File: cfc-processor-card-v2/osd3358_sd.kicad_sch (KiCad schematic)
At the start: 98 parts, among them J100 DM3BT-DSF-PEJS, J3 CONN_03LONGPADS, U11 TCAN330, U17 25AAXX, U2 DS90CR218AMTD/NOPBMTD48_TEX-L, U3 THGBMJG7C2LBAU8, U7 OSD3358-512M-BSM

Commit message: Clean up CFC Processor Card from Scott's initial import which was Gerber identical to origianl EAGLE schematic. Interestingly, this version was already changed for the v2 backplane which is great. Align schematic to be more KiCAD like based off of the C3, rename a few things, remove some outdated OPD connections, import sch into pcb, clean up pcb detritus, and import DRU settings. No longer Gerber identicial, but it's now ready for further polishing for fabrication.
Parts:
- removed J3: CONN_03LONGPADS, cfc-card:1X03_LONGPADS, symbol cfc-card-eagle-import:CONN_03LONGPADS
- removed JP2: JUMPER-SMT_3_1-NC_TRACE_SILK, cfc-card:SMT-JUMPER_3_1-NC_TRACE_SILK, symbol cfc-card-eagle-import:JUMPER-SMT_3_1-NC_TRACE_SILK
- removed R14: DNP, cfc-card:.0603-A, symbol cfc-card-eagle-import:R-US_0603-A
- removed R16, R17: 100k, cfc-card:RES_EXB2HV, symbol cfc-card-eagle-import:EXB-2HV103JV
- removed SB0, SB1, SB10, SB11, SB12, SB13, SB14, SB15, SB2, SB3, SB4, SB5, SB6, SB7, SB8, SB9: TEST-POINT-SMALL, cfc-card:TEST-POINT-SMALL, symbol cfc-card-eagle-import:TEST-POINT-SMALL
- removed unit 4 of U7
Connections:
- no-connect marks 64 -> 44
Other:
- note removed: "Boot SD SYSBOOT[4 : 0] == 0b11000 SPI0 -> MMC0 -> USB0 -> UART0 Boot eMMC SYSBOOT[4 : 0] == 0b11100 MMC1 -> MMC0 -> UART0 -> USB0"
- note removed: "Default Sysboot Pins SYSBOOT[4 : 0] == 0b11x00 SYSBOOT[2] HIGH == eMMC SYSBOOT[2] LOW == SD Card"
- note removed: "PIRT1280 Enable and TEC enable GPIO. We are using these pins because they are free and are the ones we used on pocketbeagle board"
- note removed: "SYSBOOT Circuit"
- note removed: "SYSBOOT Jumper to config boot order must use very light pullups because boot config is latched at boot and then the pins a used for other purposes"
- note removed: "SYSBOOT2 pulled high by default to boot eMMC. Manual jumper here to override"
- note removed: "SYSBOOT[15 : 5] == 0b0100_0000_000"
- company: (none) -> Portland State Aerospace Society
- title: (none) -> OreSat CFC Processor Card
- moved on the sheet: C1, C10, C11, C12, C16, C17, C2, C20, C21, C23, C24, C25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

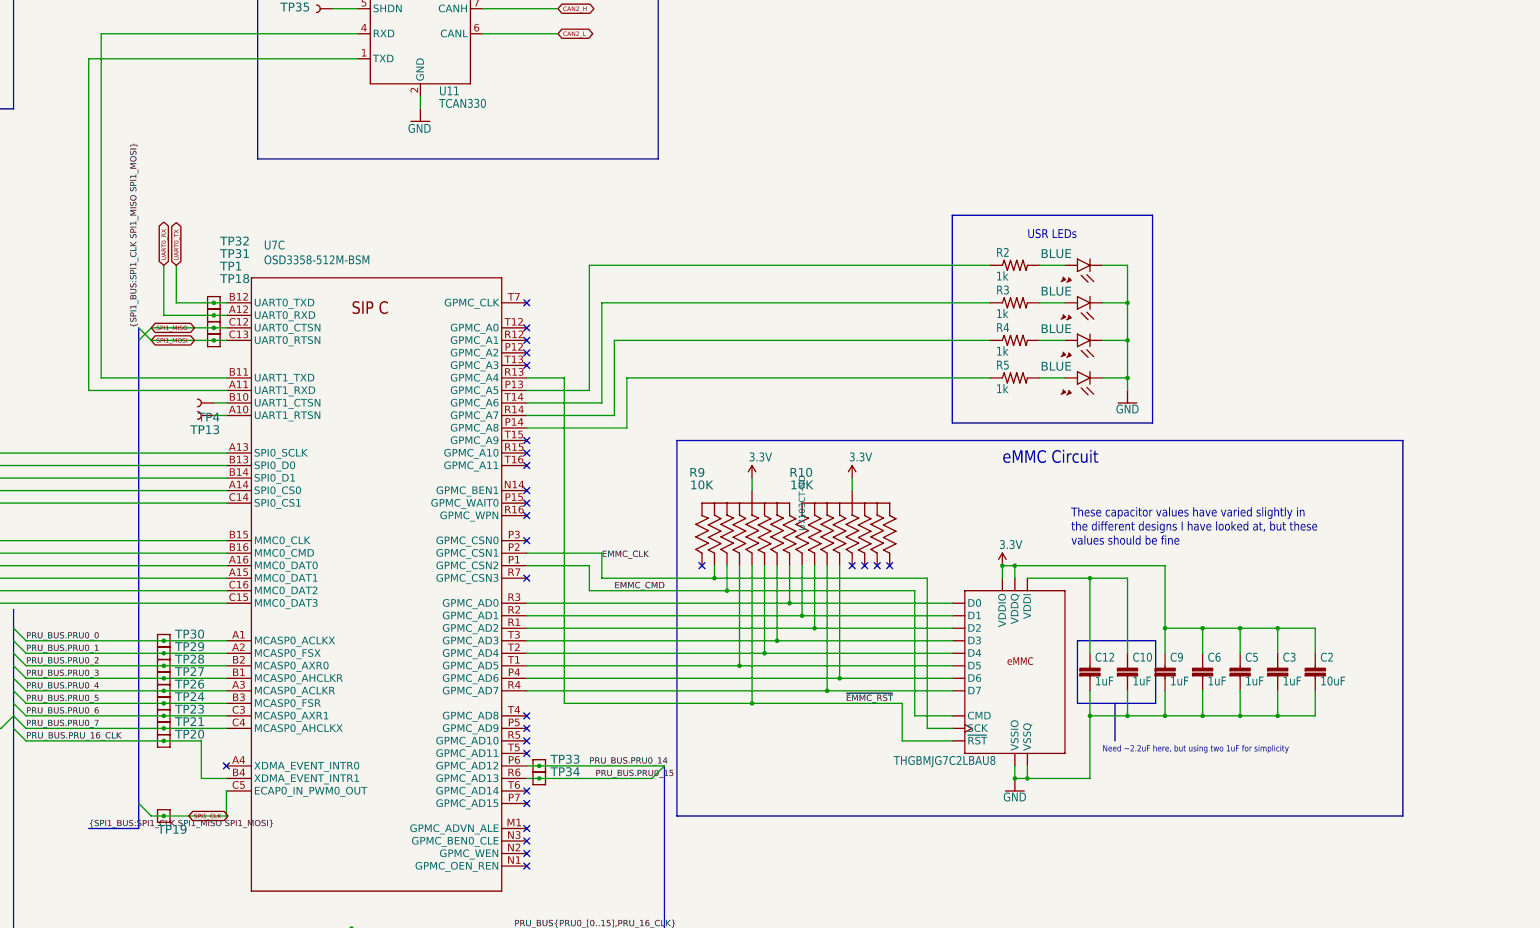
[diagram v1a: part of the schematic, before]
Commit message: Big cleanup - fixed a billion ERCs and DRCs. Switched a bunch of parts over to OreSat parts. Added analog switch on UART so CFC processor can talk serial to C3. Last thing left: clean up passives with new footprints, maybe.
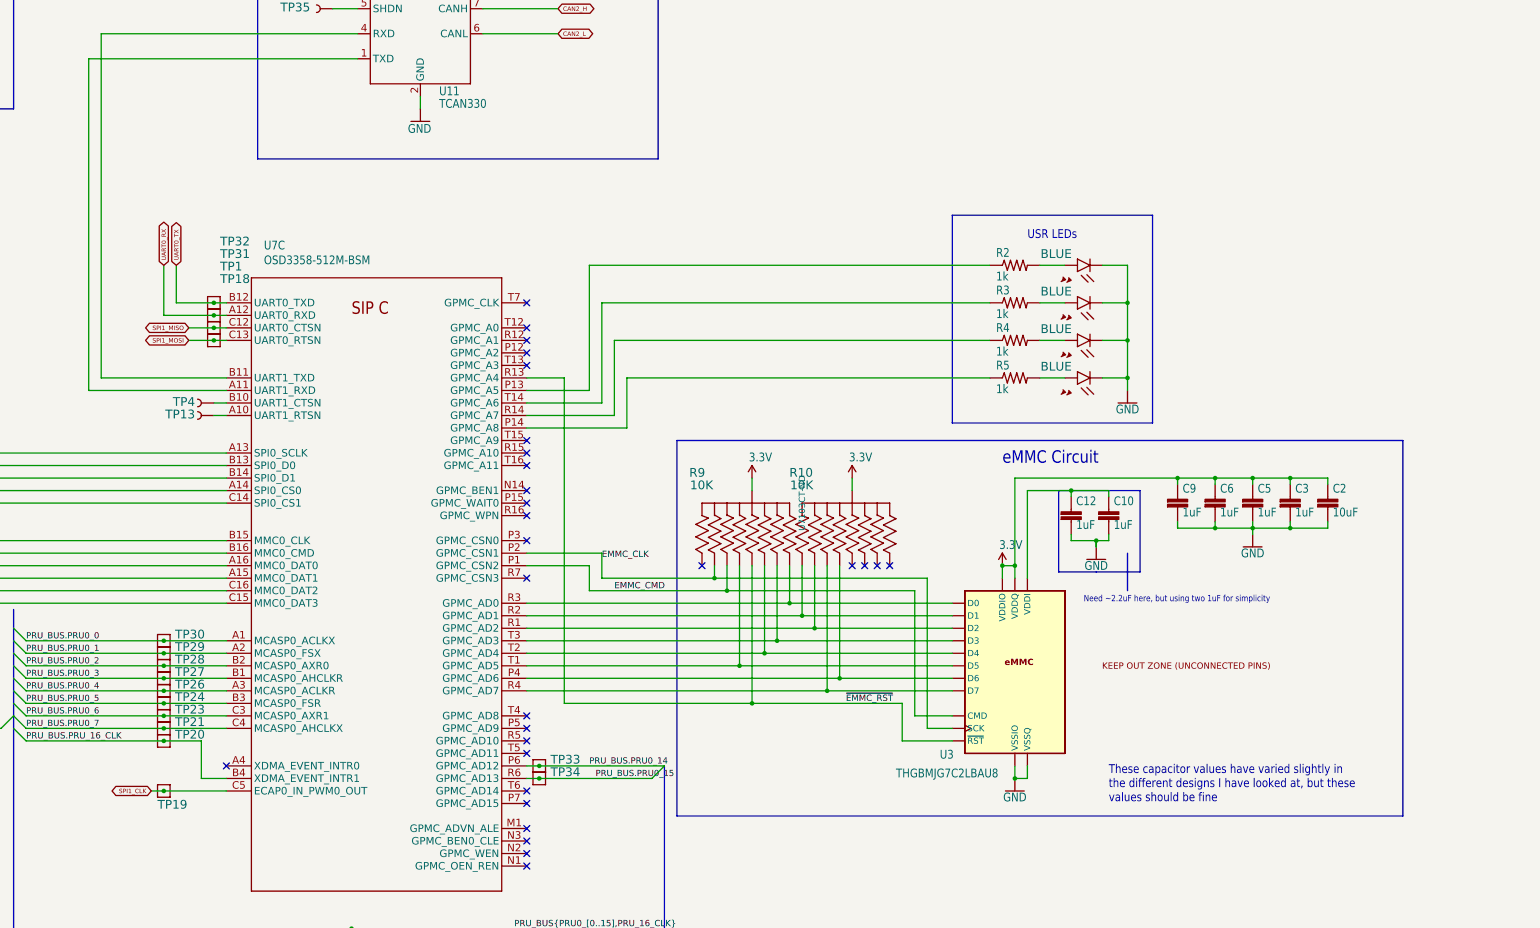
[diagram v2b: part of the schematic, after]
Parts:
- U3: footprint cfc-card:BGA-153(11.5X13)(EMMC-BA) -> oresat-ics:BGA-153(11.5X13)(EMMC-BA); symbol cfc-card-eagle-import:EMMC+RESET+5.1-COMPATIBLE-BA -> oresat-ics:EMMC+RESET+5.1-COMPATIBLE-BA
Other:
- moved on the sheet: C10, C12, C2, C3, C5, C6, C9, TP19

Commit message: more trace polishing.
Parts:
- C1, C16, C17, C20, C21, C23, C24, C25, C26, C27, C28, C42, C43, C45, C46, C47, C48, C7, R29, R30, R6, R7: footprint cfc-card:.0402-C-NOSILK -> oresat-passives:0402-C-NOSILK
- C10, C11, C12, C3, C31, C40, C5, C6, C9, R11, R2, R3, R4, R5, R59, R60: footprint cfc-card:.0603-A -> oresat-passives:0603-C-NOSILK
- C2, C8: footprint cfc-card:.0805-B -> oresat-passives:0805-C-NOSILK
- C49: footprint cfc-card:.0603-C-NOSILK -> oresat-passives:0603-C-NOSILK
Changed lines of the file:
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@@
 			)
 		)
-		(property "Footprint" "cfc-card:.0402-C-NOSILK"
+		(property "Footprint" "oresat-passives:0402-C-NOSILK"
 			(at 127 320.04 0)
 			(effects
@@
 			)
 		)
-		(property "Footprint" "cfc-card:.0805-B"
+		(property "Footprint" "oresat-passives:0805-C-NOSILK"
 			(at 393.7 171.45 0)
 			(effects
@@
 			)
 		)
-		(property "Footprint" "cfc-card:.0402-C-NOSILK"
+		(property "Footprint" "oresat-passives:0402-C-NOSILK"
 			(at 88.9 320.04 0)
 			(effects
@@
 			)
 		)
-		(property "Footprint" "cfc-card:.0603-A"
+		(property "Footprint" "oresat-passives:0603-C-NOSILK"
 			(at 40.64 64.77 0)
 			(effects
@@
 			)
 		)
-		(property "Footprint" "cfc-card:.0603-C-NOSILK"
+		(property "Footprint" "oresat-passives:0603-C-NOSILK"
 			(at 114.3 302.26 0)
 			(effects
@@
 			)
 		)
-		(property "Footprint" "cfc-card:.0603-A"
+		(property "Footprint" "oresat-passives:0603-C-NOSILK"
 			(at 330.2 124.46 0)
 			(effects
@@
 			)
 		)
-		(property "Footprint" "cfc-card:.0402-C-NOSILK"
+		(property "Footprint" "oresat-passives:0402-C-NOSILK"
 			(at 134.62 337.82 0)
 			(effects
@@
 			)
 		)
-		(property "Footprint" "cfc-card:.0603-A"
+		(property "Footprint" "oresat-passives:0603-C-NOSILK"
 			(at 370.84 171.45 0)
 			(effects
@@
 			)
 		)
-		(property "Footprint" "cfc-card:.0402-C-NOSILK"
+		(property "Footprint" "oresat-passives:0402-C-NOSILK"
 			(at 66.04 398.78 0)
 			(effects
@@
 			)
 		)
-		(property "Footprint" "cfc-card:.0402-C-NOSILK"
+		(property "Footprint" "oresat-passives:0402-C-NOSILK"
 			(at 66.04 383.54 0)
 			(effects
@@
 			)
 		)
-		(property "Footprint" "cfc-card:.0402-C-NOSILK"
+		(property "Footprint" "oresat-passives:0402-C-NOSILK"
 			(at 134.62 320.04 0)
 			(effects
@@
 			)
 		)
-		(property "Footprint" "cfc-card:.0402-C-NOSILK"
+		(property "Footprint" "oresat-passives:0402-C-NOSILK"
 			(at 88.9 337.82 0)
 			(effects
@@
 			)
 		)
-		(property "Footprint" "cfc-card:.0402-C-NOSILK"
+		(property "Footprint" "oresat-passives:0402-C-NOSILK"
 			(at 149.86 355.6 0)
 			(effects
@@
 			)
 		)
-		(property "Footprint" "cfc-card:.0603-A"
+		(property "Footprint" "oresat-passives:0603-C-NOSILK"
 			(at 363.22 171.45 0)
 			(effects
@@
 			)
 		)
-		(property "Footprint" "cfc-card:.0402-C-NOSILK"
+		(property "Footprint" "oresat-passives:0402-C-NOSILK"
 			(at 96.52 337.82 0)
 			(effects
@@
 			)
 		)
-		(property "Footprint" "cfc-card:.0402-C-NOSILK"
+		(property "Footprint" "oresat-passives:0402-C-NOSILK"
 			(at 96.52 320.04 0)
 			(effects
@@
 			)
 		)
-		(property "Footprint" "cfc-card:.0402-C-NOSILK"
+		(property "Footprint" "oresat-passives:0402-C-NOSILK"
 			(at 104.14 320.04 0)
 			(effects
@@
 			)
 		)
-		(property "Footprint" "cfc-card:.0402-C-NOSILK"
+		(property "Footprint" "oresat-passives:0402-C-NOSILK"
 			(at 73.66 355.6 0)
 			(effects
@@
 			)
 		)
-		(property "Footprint" "cfc-card:.0402-C-NOSILK"
+		(property "Footprint" "oresat-passives:0402-C-NOSILK"
 			(at 157.48 355.6 0)
 			(effects
@@
 			)
 		)
-		(property "Footprint" "cfc-card:.0603-A"
+		(property "Footprint" "oresat-passives:0603-C-NOSILK"
 			(at 330.2 132.08 0)
 			(effects
@@
 			)
 		)
-		(property "Footprint" "cfc-card:.0402-C-NOSILK"
+		(property "Footprint" "oresat-passives:0402-C-NOSILK"
 			(at 142.24 320.04 0)
 			(effects
@@
 			)
 		)
-		(property "Footprint" "cfc-card:.0603-A"
+		(property "Footprint" "oresat-passives:0603-C-NOSILK"
 			(at 40.64 74.93 0)
 			(effects
@@
 			)
 		)
-		(property "Footprint" "cfc-card:.0603-A"
+		(property "Footprint" "oresat-passives:0603-C-NOSILK"
 			(at -93.98 187.96 0)
 			(effects
@@
 			)
 		)
-		(property "Footprint" "cfc-card:.0603-A"
+		(property "Footprint" "oresat-passives:0603-C-NOSILK"
 			(at 378.46 171.45 0)
 			(effects
@@
 			)
 		)
-		(property "Footprint" "cfc-card:.0603-A"
+		(property "Footprint" "oresat-passives:0603-C-NOSILK"
 			(at 227.33 59.69 0)
 			(effects
@@
 			)
 		)
-		(property "Footprint" "cfc-card:.0402-C-NOSILK"
+		(property "Footprint" "oresat-passives:0402-C-NOSILK"
 			(at 81.28 355.6 0)
 			(effects
@@
 			)
 		)
-		(property "Footprint" "cfc-card:.0402-C-NOSILK"
+		(property "Footprint" "oresat-passives:0402-C-NOSILK"
 			(at 66.04 406.4 0)
 			(effects
@@
 			)
 		)
-		(property "Footprint" "cfc-card:.0402-C-NOSILK"
+		(property "Footprint" "oresat-passives:0402-C-NOSILK"
 			(at 142.24 337.82 0)
 			(effects
@@
 			)
 		)
-		(property "Footprint" "cfc-card:.0805-B"
+		(property "Footprint" "oresat-passives:0805-C-NOSILK"
 			(at -104.14 187.96 0)
 			(effects
@@
 			)
 		)
-		(property "Footprint" "cfc-card:.0402-C-NOSILK"
+		(property "Footprint" "oresat-passives:0402-C-NOSILK"
 			(at 149.86 337.82 0)
 			(effects
@@
 			)
 		)
-		(property "Footprint" "cfc-card:.0603-A"
+		(property "Footprint" "oresat-passives:0603-C-NOSILK"
 			(at 349.25 173.99 0)
 			(effects
@@
 			)
 		)
-		(property "Footprint" "cfc-card:.0402-C-NOSILK"
+		(property "Footprint" "oresat-passives:0402-C-NOSILK"
 			(at 88.9 355.6 0)
 			(effects
@@
 			)
 		)
-		(property "Footprint" "cfc-card:.0603-A"
+		(property "Footprint" "oresat-passives:0603-C-NOSILK"
 			(at 116.84 67.31 0)
 			(effects
@@
 			)
 		)
-		(property "Footprint" "cfc-card:.0603-A"
+		(property "Footprint" "oresat-passives:0603-C-NOSILK"
 			(at 330.2 147.32 0)
 			(effects
@@
 			)
 		)
-		(property "Footprint" "cfc-card:.0603-A"
+		(property "Footprint" "oresat-passives:0603-C-NOSILK"
 			(at 330.2 139.7 0)
 			(effects
@@
 			)
 		)
-		(property "Footprint" "cfc-card:.0603-A"
+		(property "Footprint" "oresat-passives:0603-C-NOSILK"
 			(at 386.08 171.45 0)
 			(effects
@@
 			)
 		)
-		(property "Footprint" "cfc-card:.0402-C-NOSILK"
+		(property "Footprint" "oresat-passives:0402-C-NOSILK"
 			(at 66.04 391.16 0)
 			(effects
@@
 			)
 		)
-		(property "Footprint" "cfc-card:.0402-C-NOSILK"
+		(property "Footprint" "oresat-passives:0402-C-NOSILK"
 			(at 142.24 355.6 0)
 			(effects
@@
 			)
 		)
-		(property "Footprint" "cfc-card:.0402-C-NOSILK"
+		(property "Footprint" "oresat-passives:0402-C-NOSILK"
 			(at 81.28 337.82 0)
 			(effects
@@
 			)
 		)
-		(property "Footprint" "cfc-card:.0603-A"
+		(property "Footprint" "oresat-passives:0603-C-NOSILK"
 			(at 105.41 223.52 0)
 			(effects
@@
 			)
 		)
-		(property "Footprint" "cfc-card:.0603-A"
+		(property "Footprint" "oresat-passives:0603-C-NOSILK"
 			(at 341.63 173.99 0)
 			(effects
